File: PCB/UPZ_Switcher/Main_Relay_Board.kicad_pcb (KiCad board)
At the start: 2 copper layers, 395 x 98 mm, 146 parts, among them K1 TQ2SA-5V-Z, K10 TQ2SA-5V-Z, K11 TQ2SA-5V-Z, K12 TQ2SA-5V-Z, K13 TQ2SA-5V-Z, K14 TQ2SA-5V-Z, K15 TQ2SA-5V-Z, K16 TQ2SA-5V-Z, K17 TQ2SA-5V-Z, K18 TQ2SA-5V-Z, K19 TQ2SA-5V-Z, K2 TQ2SA-5V-Z, K20 TQ2SA-5V-Z, K3 TQ2SA-5V-Z, K4 TQ2SA-5V-Z, K5 TQ2SA-5V-Z, K6 TQ2SA-5V-Z, K7 TQ2SA-5V-Z, K8 TQ2SA-5V-Z, K9 TQ2SA-5V-Z, Q1 BS170F, Q10 BS170F, Q11 BS170F, Q12 BS170F, Q13 BS170F, Q14 BS170F, Q15 BS170F, Q16 BS170F, Q17 BS170F, Q18 BS170F, Q19 BS170F, Q2 BS170F, Q20 BS170F, Q3 BS170F, Q4 BS170F, Q5 BS170F, Q6 BS170F, Q7 BS170F, Q8 BS170F, Q9 BS170F, U1 MCP23017_SP, U2 MCP23017_SP, U3 MCP23017_SP

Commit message: Relay Board finished
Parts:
- added J2: 71918-110LF, BVKSound:71918-110LF, F.Cu at (148.6, 99.7)
- R1: moved to F.Cu
- U1: footprint Package_SO:SOIC-28W_7.5x17.9mm_P1.27mm -> Package_DIP:DIP-28_W7.62mm_Socket_LongPads; moved to F.Cu
- U2, U3: footprint Package_SO:SOIC-28W_7.5x17.9mm_P1.27mm -> Package_DIP:DIP-28_W7.62mm_Socket_LongPads
- moved R1 146.5 mm to (209.6, 104.4)
- moved U1 137.8 mm to (215.8, 108.2), turned to 90 degrees
- moved U2 58.6 mm to (63.5, 108.2), turned to 90 degrees
- moved R18 51.4 mm to (57.3, 104.4)
- moved R19 43.4 mm to (316.2, 104.3)
- moved U3 37.9 mm to (322.3, 108.2), turned to 90 degrees
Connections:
- net /I2C_SCK renamed I2C_SCK
- net /I2C_SDA renamed I2C_SDA
- net Net-(R12-Pad2) renamed MCP2.8
- net Net-(R26-Pad2) renamed MCP1.1
- net Net-(R5-Pad2) renamed MCP2.7
- net Net-(U3-Pad21) renamed MCP3.9
- net Net-(U3-Pad22) renamed MCP3.10
- net Net-(U3-Pad23) renamed MCP3.11
- net Net-(U3-Pad24) renamed MCP3.12
- BUS_B1 pad MH1: /Relay/BUSBMH -> /Relay/BUSAMH
- Input_1 pad 4: /Relay/IN1.4 -> /Relay/BUSAMH
- Input_2 pad 4: /Relay/IN2.4 -> /Relay/BUSAMH
- Input_3 pad 4: /Relay/IN3.4 -> /Relay/BUSAMH
- Input_4 pad 4: /Relay/IN4.4 -> /Relay/BUSAMH
- Input_5 pad 4: /Relay/IN5.4 -> /Relay/BUSAMH
- Input_6 pad 4: /Relay/IN6.4 -> /Relay/BUSAMH
- Input_7 pad 4: /Relay/IN7.4 -> /Relay/BUSAMH
- Input_8 pad 4: /Relay/IN8.4 -> /Relay/BUSAMH
- R1 pad 2: /VDD -> K1+
- R10 pad 2: Net-(R10-Pad2) -> MCP3.4
- R11 pad 2: Net-(R11-Pad2) -> MCP1.16
- R13 pad 2: Net-(R13-Pad2) -> MCP1.8
- R14 pad 2: Net-(R14-Pad2) -> MCP1.11
- R15 pad 2: Net-(R15-Pad2) -> MCP1.12
- R16 pad 2: Net-(R16-Pad2) -> MCP2.12
- R17 pad 2: Net-(R17-Pad2) -> MCP1.4
- R18 pad 2: /VDD -> K1+
- R19 pad 2: /VDD -> K1+
- R2 pad 2: Net-(R2-Pad2) -> MCP2.15
- R20 pad 2: Net-(R20-Pad2) -> MCP2.3
- R21 pad 2: Net-(R21-Pad2) -> MCP3.7
- R22 pad 1: Net-(R22-Pad1) -> MCP2.4
- R23 pad 1: Net-(R23-Pad1) -> MCP3.8
- R24 pad 2: Net-(R24-Pad2) -> MCP1.2
- R25 pad 2: Net-(R25-Pad2) -> MCP2.6
- R27 pad 2: Net-(R27-Pad2) -> MCP2.5
- R28 pad 2: Net-(R28-Pad2) -> MCP1.6
- R29 pad 2: Net-(R29-Pad2) -> MCP2.10
- R3 pad 2: Net-(R3-Pad2) -> MCP3.3
- R30 pad 2: Net-(R30-Pad2) -> MCP1.5
- R31 pad 2: Net-(R31-Pad2) -> MCP2.9
- R32 pad 2: Net-(R32-Pad2) -> MCP1.10
- R33 pad 2: Net-(R33-Pad2) -> MCP2.14
- R34 pad 2: Net-(R34-Pad2) -> MCP1.9
- R35 pad 2: Net-(R35-Pad2) -> MCP2.13
- R36 pad 2: Net-(R36-Pad2) -> MCP2.2
- R37 pad 2: Net-(R37-Pad2) -> MCP1.14
- R38 pad 2: Net-(R38-Pad2) -> MCP3.2
- R39 pad 2: Net-(R39-Pad2) -> MCP1.13
- R4 pad 2: Net-(R4-Pad2) -> MCP1.15
- R40 pad 2: Net-(R40-Pad2) -> MCP3.1
- R41 pad 2: Net-(R41-Pad2) -> MCP3.6
- R42 pad 2: Net-(R42-Pad2) -> MCP2.1
- R43 pad 2: Net-(R43-Pad2) -> MCP3.5
- R6 pad 2: Net-(R6-Pad2) -> MCP2.11
- R7 pad 2: Net-(R7-Pad2) -> MCP2.16
- R8 pad 2: Net-(R8-Pad2) -> MCP1.3
- R9 pad 2: Net-(R9-Pad2) -> MCP1.7
- U1 pad 1: Net-(R2-Pad2) -> MCP2.1
- U1 pad 16: /VDD -> K1+
- U1 pad 2: Net-(R7-Pad2) -> MCP2.2
- U1 pad 21: Net-(R6-Pad2) -> MCP2.9
- U1 pad 22: Net-(R16-Pad2) -> MCP2.10
- U1 pad 23: Net-(R9-Pad2) -> MCP2.11
- U1 pad 24: Net-(R13-Pad2) -> MCP2.12
- U1 pad 25: Net-(R14-Pad2) -> MCP2.13
- U1 pad 26: Net-(R15-Pad2) -> MCP2.14
- U1 pad 27: Net-(R8-Pad2) -> MCP2.15
- U1 pad 28: Net-(R17-Pad2) -> MCP2.16
- U1 pad 3: Net-(R3-Pad2) -> MCP2.3
- U1 pad 4: Net-(R10-Pad2) -> MCP2.4
- U1 pad 5: Net-(R4-Pad2) -> MCP2.5
- U1 pad 6: Net-(R11-Pad2) -> MCP2.6
- U1 pad 9: /VDD -> K1+
- U2 pad 2: Net-(R30-Pad2) -> MCP1.2
- U2 pad 21: Net-(R24-Pad2) -> MCP1.9
- U2 pad 22: Net-(R28-Pad2) -> MCP1.10
- U2 pad 23: Net-(R32-Pad2) -> MCP1.11
- U2 pad 24: Net-(R37-Pad2) -> MCP1.12
- U2 pad 25: Net-(R25-Pad2) -> MCP1.13
- U2 pad 26: Net-(R29-Pad2) -> MCP1.14
- U2 pad 27: Net-(R33-Pad2) -> MCP1.15
- U2 pad 28: Net-(R38-Pad2) -> MCP1.16
- U2 pad 3: Net-(R34-Pad2) -> MCP1.3
- U2 pad 4: Net-(R39-Pad2) -> MCP1.4
- U2 pad 5: Net-(R27-Pad2) -> MCP1.5
- U2 pad 6: Net-(R31-Pad2) -> MCP1.6
- U2 pad 7: Net-(R35-Pad2) -> MCP1.7
- U2 pad 8: Net-(R40-Pad2) -> MCP1.8
- U2 pad 9: /VDD -> K1+
- U3 pad 1: Net-(R36-Pad2) -> MCP3.1
- U3 pad 15: /VDD -> K1+
- U3 pad 2: Net-(R41-Pad2) -> MCP3.2
- U3 pad 25: Net-(R20-Pad2) -> MCP3.13
- U3 pad 26: Net-(R22-Pad1) -> MCP3.14
- U3 pad 27: Net-(R21-Pad2) -> MCP3.15
- U3 pad 28: Net-(R23-Pad1) -> MCP3.16
- U3 pad 3: Net-(R42-Pad2) -> MCP3.3
- U3 pad 4: Net-(R43-Pad2) -> MCP3.4
- U3 pad 5: Net-(U3-Pad5) -> MCP3.5
- U3 pad 6: Net-(U3-Pad6) -> MCP3.6
- U3 pad 7: Net-(U3-Pad7) -> MCP3.7
- U3 pad 8: Net-(U3-Pad8) -> MCP3.8
- U3 pad 9: /VDD -> K1+
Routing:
- net Net-(R3-Pad2): track 337.4 -> 0.00 mm
- net Net-(R2-Pad2): track 304.6 -> 0.00 mm
- net Net-(R7-Pad2): track 303.0 -> 0.00 mm
- net GND: track 1145.0 -> 1436.5 mm, vias 35 -> 45
- net I2C_SCK: track 13.5 -> 295.2 mm, vias 0 -> 4
- net I2C_SDA: track 11.6 -> 291.4 mm
- net Net-(R42-Pad2): track 277.6 -> 0.00 mm, vias 3 -> 0
- net Net-(R10-Pad2): track 276.1 -> 0.00 mm
- net Net-(R20-Pad2): track 270.9 -> 0.00 mm, vias 1 -> 0
- net Phantom_48V_HOT_B: track 0.00 -> 270.5 mm, vias 0 -> 3
- net Net-(R22-Pad1): track 268.1 -> 0.00 mm, vias 3 -> 0
- net Net-(R16-Pad2): track 259.0 -> 0.00 mm
- net Net-(R6-Pad2): track 257.0 -> 0.00 mm
- net Net-(R36-Pad2): track 256.0 -> 0.00 mm, vias 3 -> 0
- net Net-(R40-Pad2): track 251.1 -> 0.00 mm, vias 1 -> 0
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- added copper zone on F.Cu, net Phantom_GND

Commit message: updated phantom design + MCU board
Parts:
- added C21: 47uF, Capacitor_THT:CP_Radial_D8.0mm_P3.50mm, F.Cu at (152.8, 171.4)
- added C22: 47uF, Capacitor_THT:CP_Radial_D8.0mm_P3.50mm, F.Cu at (156.2, 181.9)
- added C23: 47uF, Capacitor_THT:CP_Radial_D8.0mm_P3.50mm, F.Cu at (347.5, 171.4)
- added C24: 47uF, Capacitor_THT:CP_Radial_D8.0mm_P3.50mm, F.Cu at (351.0, 181.9)
- added R44: 6K8, Resistor_SMD:R_1206_3216Metric, B.Cu at (183.8, 129.1)
- added R45: 6K8, Resistor_SMD:R_1206_3216Metric, B.Cu at (166.9, 129.1)
- added R46: 6K8, Resistor_SMD:R_1206_3216Metric, B.Cu at (378.8, 129.3)
- added R47: 6K8, Resistor_SMD:R_1206_3216Metric, B.Cu at (362.3, 129.1)
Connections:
- net Phantom_GND renamed Phantom_48V_GND
- J2 pad 6: Phantom_48V_HOT_A -> Phantom_48V
- J2 pad 7: Phantom_48V_COLD_A -> Net-(J2-Pad7)
- J2 pad 8: Phantom_48V_HOT_B -> Net-(J2-Pad8)
- J2 pad 9: Phantom_48V_COLD_B -> Net-(J2-Pad9)
- K10 pad 3: Phantom_48V_HOT_B -> Net-(K10-Pad3)
- K10 pad 8: Phantom_48V_COLD_B -> Net-(K10-Pad8)
- K19 pad 3: /Relay/OUTA.2 -> Net-(C22-Pad2)
- K19 pad 8: /Relay/OUTA.3 -> Net-(C21-Pad2)
- K20 pad 3: /Relay/OUTB.2 -> Net-(C24-Pad2)
- K20 pad 8: /Relay/OUTB.3 -> Net-(C23-Pad2)
- K5 pad 3: Phantom_48V_HOT_A -> Net-(K5-Pad3)
- K5 pad 8: Phantom_48V_COLD_A -> Net-(K5-Pad8)
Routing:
- net Phantom_48V: track 0.00 -> 354.9 mm, vias 0 -> 7
- net Phantom_48V_HOT_B: track 270.5 -> 0.00 mm, vias 3 -> 0
- net Phantom_48V_COLD_B: track 248.8 -> 0.00 mm, vias 3 -> 0
- net Phantom_48V_HOT_A: track 71.7 -> 0.00 mm, vias 3 -> 0
- net Net-(C22-Pad2): track 0.00 -> 69.5 mm
- net Net-(C24-Pad2): track 0.00 -> 68.1 mm
- net Phantom_48V_COLD_A: track 56.4 -> 0.00 mm, vias 2 -> 0
- net Net-(C21-Pad2): track 0.00 -> 33.1 mm
- net Net-(C23-Pad2): track 0.00 -> 32.8 mm
- net /Relay/OUTB.2: track 20.4 -> 33.9 mm
- net /Relay/OUTA.2: track 20.3 -> 33.3 mm
- net Phantom_48V_GND: track 103.6 -> 94.0 mm
- net GND: track 1436.5 -> 1427.3 mm
- net Net-(K10-Pad3): track 0.00 -> 9.10 mm, vias 0 -> 1
- net Net-(K5-Pad8): track 0.00 -> 9.05 mm, vias 0 -> 1
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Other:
- board size 395 x 98 mm -> 373 x 98 mm

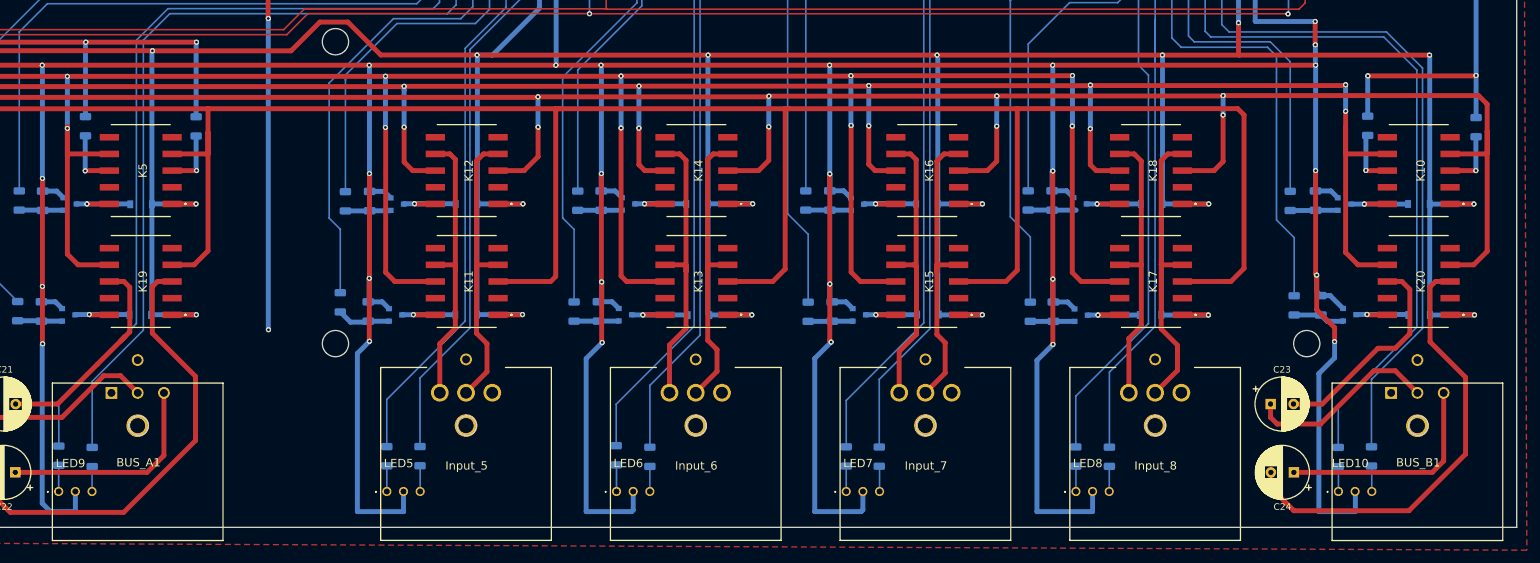
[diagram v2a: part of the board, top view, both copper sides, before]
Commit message: update on power supply
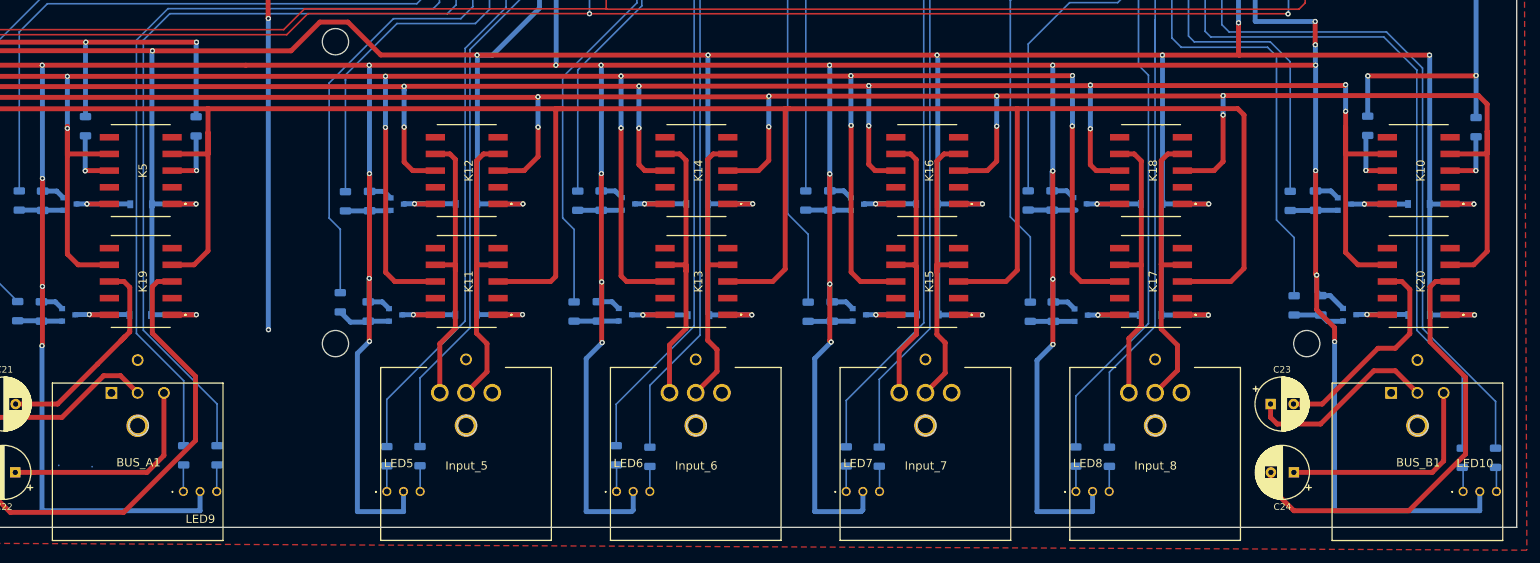
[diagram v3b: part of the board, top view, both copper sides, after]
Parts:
- moved R22 19.0 mm to (186.9, 179.3)
- moved R20 19.0 mm to (181.9, 179.3)
- moved LED10 19.0 mm to (379.3, 184.8)
- moved LED9 19.0 mm to (184.3, 184.8)
- moved R23 18.9 mm to (381.8, 179.6)
- moved R21 18.9 mm to (376.7, 179.6)
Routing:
- net GND: track 1427.3 -> 1461.9 mm
- net MCP3.7: track 103.6 -> 101.6 mm
- net MCP2.3: track 117.3 -> 115.4 mm
- net MCP3.8: track 99.7 -> 101.3 mm
- net MCP2.4: track 117.6 -> 118.8 mm

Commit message: final
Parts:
- moved C22 43.8 mm to (196.6, 165.0)
- moved C21 6.49 mm to (152.9, 165.0)
- moved C24 2.17 mm to (351.3, 179.7)
- moved C23 2.16 mm to (347.9, 169.3)
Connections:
- BUS_B1 pad G1: /Relay/BUSA.G -> /Relay/BUSB.G
- BUS_B1 pad MH1: /Relay/BUSAMH -> /Relay/BUSBMH
- C21 pad 1: /Relay/OUTA.3 -> /Relay/OUTA.2
- C22 pad 1: /Relay/OUTA.2 -> /Relay/OUTA.3
- C23 pad 1: /Relay/OUTB.3 -> /Relay/OUTB.2
- C24 pad 1: /Relay/OUTB.2 -> /Relay/OUTB.3
- Input_1 pad 4: /Relay/BUSAMH -> /Relay/IN1.4
- Input_1 pad 5: /Relay/BUSA.G -> /Relay/IN1.5
- Input_2 pad 4: /Relay/BUSAMH -> /Relay/IN2.4
- Input_2 pad 5: /Relay/BUSA.G -> /Relay/IN2.5
- Input_3 pad 4: /Relay/BUSAMH -> /Relay/IN3.4
- Input_3 pad 5: /Relay/BUSA.G -> /Relay/IN3.5
- Input_4 pad 4: /Relay/BUSAMH -> /Relay/IN4.4
- Input_4 pad 5: /Relay/BUSA.G -> /Relay/IN4.5
- Input_5 pad 4: /Relay/BUSAMH -> /Relay/IN5.4
- Input_5 pad 5: /Relay/BUSA.G -> /Relay/IN5.5
- Input_6 pad 4: /Relay/BUSAMH -> /Relay/IN6.4
- Input_6 pad 5: /Relay/BUSA.G -> /Relay/IN6.5
- Input_7 pad 4: /Relay/BUSAMH -> /Relay/IN7.4
- Input_7 pad 5: /Relay/BUSA.G -> /Relay/IN7.5
- Input_8 pad 4: /Relay/BUSAMH -> /Relay/IN8.4
- Input_8 pad 5: /Relay/BUSA.G -> /Relay/IN8.5
- K1 pad 3: /Relay/BUSA.2 -> /Relay/BUSA.3
- K1 pad 4: /Relay/IN1.2 -> /Relay/IN1.3
- K1 pad 7: /Relay/IN1.3 -> /Relay/IN1.2
- K1 pad 8: /Relay/BUSA.3 -> /Relay/BUSA.2
- K10 pad 4: /Relay/BUSB.2 -> /Relay/BUSB.3
- K10 pad 7: /Relay/BUSB.3 -> /Relay/BUSB.2
- K11 pad 3: /Relay/BUSA.2 -> /Relay/BUSA.3
- K11 pad 4: /Relay/IN5.2 -> /Relay/IN5.3
- K11 pad 7: /Relay/IN5.3 -> /Relay/IN5.2
- K11 pad 8: /Relay/BUSA.3 -> /Relay/BUSA.2
- K12 pad 3: /Relay/BUSB.2 -> /Relay/BUSB.3
- K12 pad 4: /Relay/IN5.2 -> /Relay/IN5.3
- K12 pad 7: /Relay/IN5.3 -> /Relay/IN5.2
- K12 pad 8: /Relay/BUSB.3 -> /Relay/BUSB.2
- K13 pad 3: /Relay/BUSA.2 -> /Relay/BUSA.3
- K13 pad 4: /Relay/IN6.2 -> /Relay/IN6.3
- K13 pad 7: /Relay/IN6.3 -> /Relay/IN6.2
- K13 pad 8: /Relay/BUSA.3 -> /Relay/BUSA.2
- K14 pad 3: /Relay/BUSB.2 -> /Relay/BUSB.3
- K14 pad 4: /Relay/IN6.2 -> /Relay/IN6.3
- K14 pad 7: /Relay/IN6.3 -> /Relay/IN6.2
- K14 pad 8: /Relay/BUSB.3 -> /Relay/BUSB.2
- K15 pad 3: /Relay/BUSA.2 -> /Relay/BUSA.3
- K15 pad 4: /Relay/IN7.2 -> /Relay/IN7.3
- K15 pad 7: /Relay/IN7.3 -> /Relay/IN7.2
- K15 pad 8: /Relay/BUSA.3 -> /Relay/BUSA.2
- K16 pad 3: /Relay/BUSB.2 -> /Relay/BUSB.3
- K16 pad 4: /Relay/IN7.2 -> /Relay/IN7.3
- K16 pad 7: /Relay/IN7.3 -> /Relay/IN7.2
- K16 pad 8: /Relay/BUSB.3 -> /Relay/BUSB.2
- K17 pad 3: /Relay/BUSA.2 -> /Relay/BUSA.3
- K17 pad 4: /Relay/IN8.2 -> /Relay/IN8.3
- K17 pad 7: /Relay/IN8.3 -> /Relay/IN8.2
- K17 pad 8: /Relay/BUSA.3 -> /Relay/BUSA.2
- K18 pad 3: /Relay/BUSB.2 -> /Relay/BUSB.3
- K18 pad 4: /Relay/IN8.2 -> /Relay/IN8.3
- K18 pad 7: /Relay/IN8.3 -> /Relay/IN8.2
- K18 pad 8: /Relay/BUSB.3 -> /Relay/BUSB.2
- K19 pad 4: /Relay/BUSA.2 -> /Relay/BUSA.3
- K19 pad 7: /Relay/BUSA.3 -> /Relay/BUSA.2
- K2 pad 3: /Relay/BUSB.2 -> /Relay/BUSB.3
- K2 pad 4: /Relay/IN1.2 -> /Relay/IN1.3
- K2 pad 7: /Relay/IN1.3 -> /Relay/IN1.2
- K2 pad 8: /Relay/BUSB.3 -> /Relay/BUSB.2
- K20 pad 4: /Relay/BUSB.2 -> /Relay/BUSB.3
- K20 pad 7: /Relay/BUSB.3 -> /Relay/BUSB.2
- K3 pad 3: /Relay/BUSA.2 -> /Relay/BUSA.3
- K3 pad 4: /Relay/IN2.2 -> /Relay/IN2.3
- K3 pad 7: /Relay/IN2.3 -> /Relay/IN2.2
- K3 pad 8: /Relay/BUSA.3 -> /Relay/BUSA.2
- K4 pad 3: /Relay/BUSB.2 -> /Relay/BUSB.3
- K4 pad 4: /Relay/IN2.2 -> /Relay/IN2.3
- K4 pad 7: /Relay/IN2.3 -> /Relay/IN2.2
- K4 pad 8: /Relay/BUSB.3 -> /Relay/BUSB.2
- K5 pad 4: /Relay/BUSA.2 -> /Relay/BUSA.3
- K5 pad 7: /Relay/BUSA.3 -> /Relay/BUSA.2
- K6 pad 3: /Relay/BUSA.2 -> /Relay/BUSA.3
- K6 pad 4: /Relay/IN3.2 -> /Relay/IN3.3
- K6 pad 7: /Relay/IN3.3 -> /Relay/IN3.2
- K6 pad 8: /Relay/BUSA.3 -> /Relay/BUSA.2
- K7 pad 3: /Relay/BUSB.2 -> /Relay/BUSB.3
- K7 pad 4: /Relay/IN3.2 -> /Relay/IN3.3
- K7 pad 7: /Relay/IN3.3 -> /Relay/IN3.2
- K7 pad 8: /Relay/BUSB.3 -> /Relay/BUSB.2
- K8 pad 3: /Relay/BUSA.2 -> /Relay/BUSA.3
- K8 pad 4: /Relay/IN4.2 -> /Relay/IN4.3
- K8 pad 7: /Relay/IN4.3 -> /Relay/IN4.2
- K8 pad 8: /Relay/BUSA.3 -> /Relay/BUSA.2
- K9 pad 3: /Relay/BUSB.2 -> /Relay/BUSB.3
- K9 pad 4: /Relay/IN4.2 -> /Relay/IN4.3
- K9 pad 7: /Relay/IN4.3 -> /Relay/IN4.2
- K9 pad 8: /Relay/BUSB.3 -> /Relay/BUSB.2
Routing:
- net Net-(C22-Pad2): track 69.5 -> 28.3 mm
- net MCP1.2: track 79.8 -> 88.7 mm
- net MCP1.1: track 85.6 -> 94.5 mm
- net /Relay/BUSB.3: track 514.7 -> 521.9 mm
- net /Relay/OUTB.3: track 29.6 -> 22.7 mm
- net /Relay/BUSA.3: track 643.8 -> 650.7 mm, vias 16 -> 18
- net /Relay/BUSB.2: track 505.6 -> 499.1 mm, vias 14 -> 16
- net /Relay/BUSA.2: track 609.3 -> 603.1 mm
- net /Relay/OUTB.2: track 33.9 -> 29.5 mm
- net I2C_SCK: track 295.2 -> 291.2 mm, vias 4 -> 3
- net /Relay/OUTA.2: track 33.3 -> 29.4 mm
- net Phantom_48V_GND: track 94.0 -> 97.1 mm
- net MCP3.2: track 41.0 -> 43.8 mm
- net /Relay/IN4.2: track 47.2 -> 44.5 mm
- net /Relay/IN4.3: track 44.5 -> 47.1 mm
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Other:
- board text added: "UPZ Switcher Relay Board BVKSound 2021-03"
